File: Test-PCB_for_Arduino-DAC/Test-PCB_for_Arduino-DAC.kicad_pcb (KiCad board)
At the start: 2 copper layers, 54 x 100 mm, 44 parts, among them J201 PWM_FWD, J202 Molex Mini-fit Jr. 39-28-1243, J203 Pinheader Controls, J301 U-Sense_int, J302 Probe_DAC_A, J303 Probe_DAC_B, J304 VFB, J401 Arduino_Pinout_01-15, J402 SPI, J403 UART, J404 A6+7, J405 I2C, J406 Arduino_Pinout_16-30, Q201 BC818, U201 STM6600, U301 MCP602, U302 MCP4822

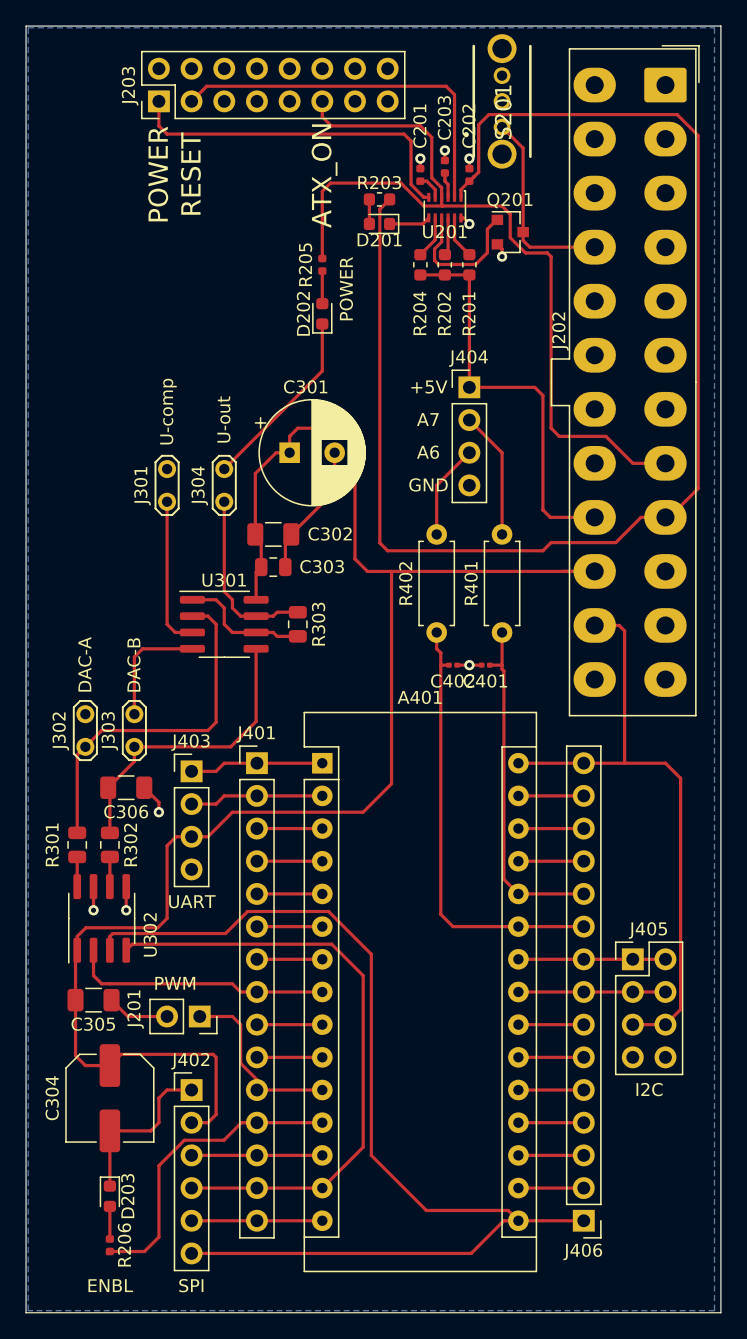
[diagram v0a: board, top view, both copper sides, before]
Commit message: Improved Test-PCB Arduino-DAC
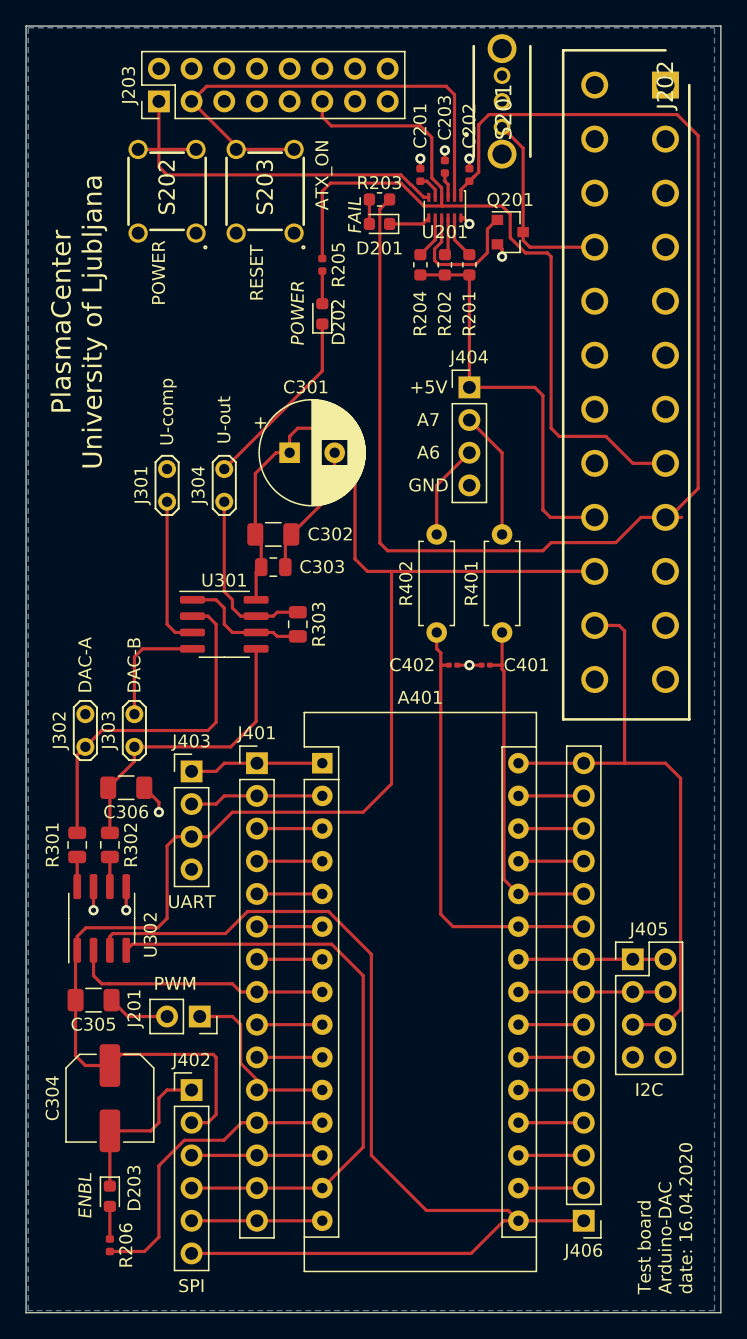
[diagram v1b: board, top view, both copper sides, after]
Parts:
- added S202: 1825910-6, SamacSys_PCB_library:1825910-6, F.Cu at (74.9, 49.5)
- added S203: 1825910-6, SamacSys_PCB_library:1825910-6, F.Cu at (82.5, 49.5)
- J202: value Molex Mini-fit Jr. 39-28-1243 -> 39-28-1243; footprint Connector_Molex:Molex_Mini-Fit_Jr_5566-24A_2x12_P4.20mm_Vertical -> SamacSys_PCB_library:SHDR24W120P550X420_2X12_5160X960X1310P
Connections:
- J202 pad 10: +12V -> GND
- J202 pad 11: +12V -> +5V
- J202 pad 12: +3V3 -> GND
- J202 pad 13: +3V3 -> GND
- J202 pad 14: (no net) -> GND
- J202 pad 15: GND -> /Plugs_and_Controls/PWR_GOOD
- J202 pad 16: /Plugs_and_Controls/PWR_ON -> (no net)
- J202 pad 17: GND -> /Plugs_and_Controls/VSB
- J202 pad 18: GND -> +5V
- J202 pad 19: GND -> +12V
- J202 pad 20: (no net) -> +5V
- J202 pad 21: +5V -> +12V
- J202 pad 23: +5V -> +3V3
- J202 pad 3: GND -> +3V3
- J202 pad 4: +5V -> (no net)
- J202 pad 6: +5V -> GND
- J202 pad 7: GND -> +5V
- J202 pad 8: /Plugs_and_Controls/PWR_GOOD -> /Plugs_and_Controls/PWR_ON
- J202 pad 9: /Plugs_and_Controls/VSB -> GND
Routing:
- net /Plugs_and_Controls/SR: track 29.2 -> 38.8 mm
- net /Plugs_and_Controls/PB: track 27.2 -> 31.5 mm
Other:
- board text added: "FAIL"
- board text added: "PlasmaCenter University of Ljubljana"
- board text added: "Test board Arduino-DAC date: 16.04.2020"
